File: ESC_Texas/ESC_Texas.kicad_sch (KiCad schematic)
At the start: 78 parts, among them IC1 nRF52840-QFAA-F-R7, IC11 LM3480IM3-3.3_NOPB, IC12 LM3480IM3-3.3_NOPB, J1 RJ45, J11 Battery+, J12 Conn_01x02, J13 Conn_01x04_Pin, J14 Conn_01x01_Pin, J15 Conn_01x01_Pin, J16 Conn_01x01_Pin, J17 Conn_01x01_Pin, J2 BD125-10-A-0305-0580-L-B, J3 Motor, J4 Conn_01x02_Pin, P0.03 TestPoint, P0.10 TestPoint, P0.11 TestPoint, P0.12 TestPoint, P0.7 TestPoint, P0.9 TestPoint, P1.0 TestPoint, P1.1 TestPoint, P1.9 TestPoint, U1 MCP2515-xSO, U2 TJA1051T, X1 CM7V-T1A-32.768kHz, X2 32MHz, X3 C115962

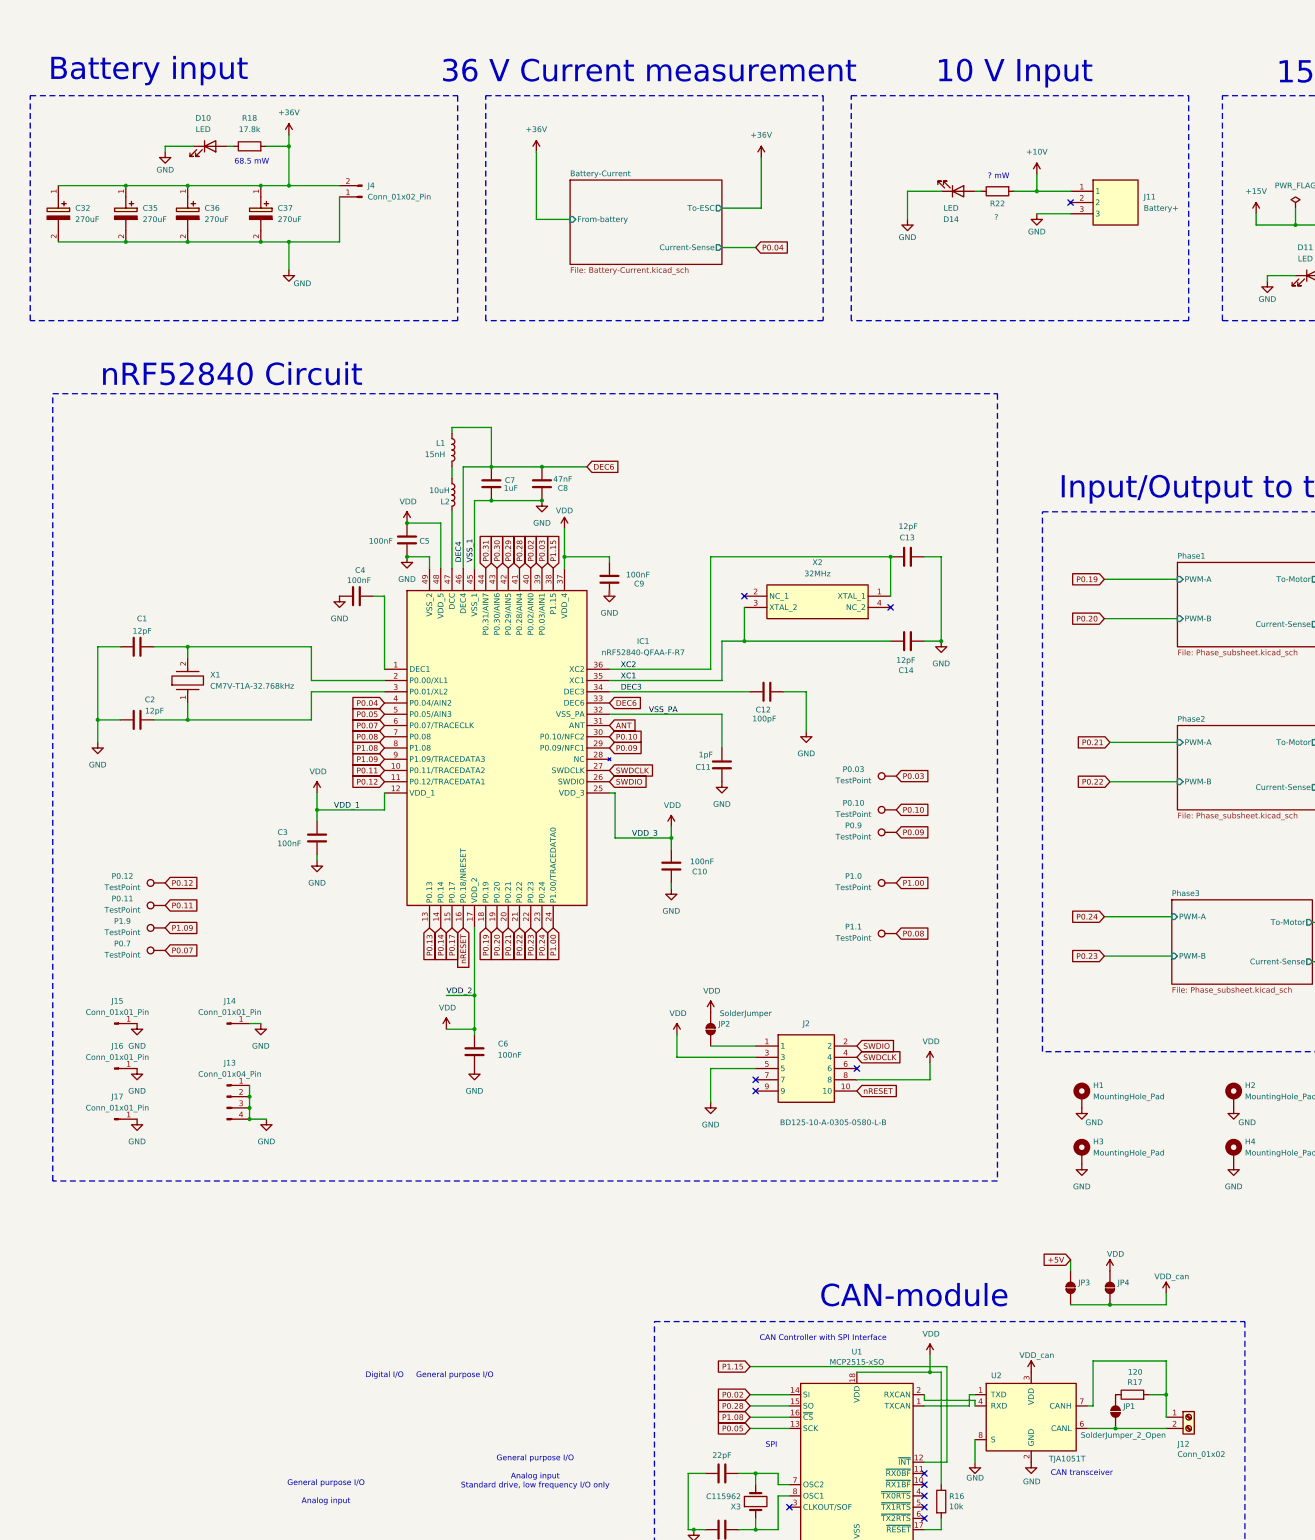
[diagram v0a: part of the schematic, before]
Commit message: Added combined CAN and 10v connector
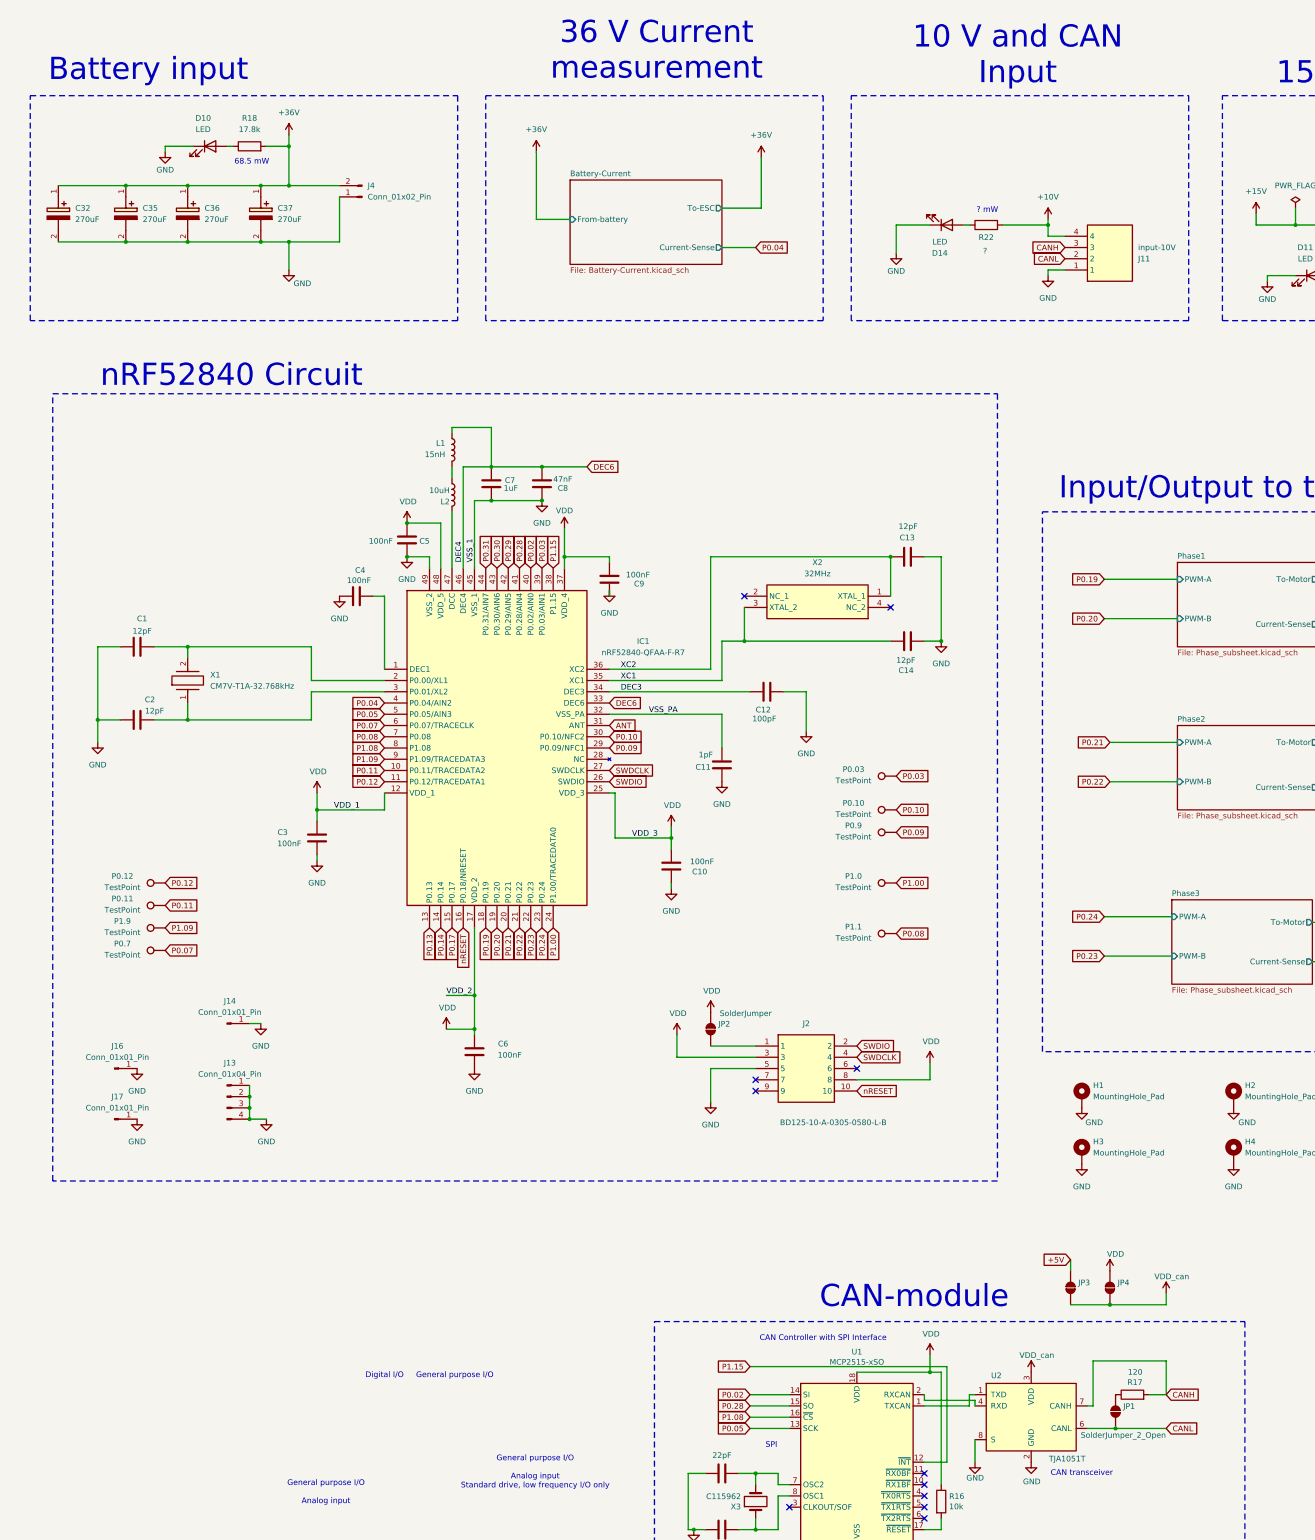
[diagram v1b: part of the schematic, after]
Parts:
- removed J12: Conn_01x02, Connector_Phoenix_MC:PhoenixContact_MCV_1,5_2-G-3.5_1x02_P3.50mm_Vertical, symbol Connector:Screw_Terminal_01x02
- removed J15: Conn_01x01_Pin, Connector_PinHeader_2.54mm:PinHeader_1x01_P2.54mm_Vertical, symbol Connector:Conn_01x01_Pin
- J11: value Battery+ -> input-10V; footprint LIB_2350514-3:SHDRRA3W90P0X350_1X3_1110X920X691P -> TBP02R1-381-04BE:TBP02R1-381-02BE
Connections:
- net +10V: now also J11.4; no longer J11.1
- net GND: now also J11.1; no longer J11.3
- net CANL: now reaches JP1.2 (B), U2.6 (CANL)
- net CANL: now also J11.2
- net CANH: now reaches R17.2, U2.7 (CANH)
- net CANH: now also J11.3
- no-connect marks 12 -> 11
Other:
- note added: "10 V and CAN Input"
- note removed: "10 V Input"
- moved on the sheet: D14, R22

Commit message: saved project
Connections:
- net +10V: now also J11.1; no longer J11.4
- net CANH: now also J11.2; no longer J11.3
- net CANL: now also J11.3; no longer J11.2
- net GND: now also J11.4; no longer J11.1
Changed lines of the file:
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@@
-	)
-	(symbol
-		(lib_name "2350514-3_1")
-		(lib_id "2350514-3:2350514-3")
-		(at 270.51 73.66 0)
-		(mirror x)
-		(unit 1)
-		(exclude_from_sim no)
-		(in_bom yes)
-		(on_board yes)
-		(dnp no)
-		(property "Reference" "J11"
-			(at 287.02 71.1201 0)
-			(effects
-				(font
-					(size 1.27 1.27)
-				)
-				(justify left)
-			)
-		)
-		(property "Value" "input-10V"
-			(at 287.02 68.5801 0)
-			(effects
-				(font
-					(size 1.27 1.27)
-				)
-				(justify left)
-			)
-		)
-		(property "Footprint" "TBP02R1-381-04BE:TBP02R1-381-02BE"
-			(at 287.02 -21.26 0)
-			(effects
-				(font
-					(size 1.27 1.27)
-				)
-				(justify left top)
-				(hide yes)
-			)
-		)
-		(property "Datasheet" "https://www.te.com/commerce/DocumentDelivery/DDEController?Action=srchrtrv&DocNm=3-1773982-8&DocType=Data%20Sheet&DocLang=English&PartCntxt=2350514-3&DocFormat=pdf"
-			(at 287.02 -121.26 0)
-			(effects
-				(font
-					(size 1.27 1.27)
-				)
-				(justify left top)
-				(hide yes)
-			)
-		)
-		(property "Description" "Body Features: Primary Product Color Green | Product Orientation Right Angle | Configuration Features: Stacking Configuration Side Stackable | Number of Rows 1 | Number of Positions 3 | Contact Features: Contact Mating Area Plating Material Tin | Contact Current Rating (Max) 10 AMP | Contact Base Material Brass | Electrical Characteristics: Operating Voltage 300 VAC | Housing Features: Housing Material PA 66 | Centerline (Pitch) .137 INCH | Centerline (Pitch) 3.5 MM | Mechanical Attachment: Connector Mounti"
-			(at 270.002 93.726 0)
-			(effects
-				(font
-					(size 1.27 1.27)
-				)
-				(hide yes)
-			)
-		)
-		(property "Height" "6.91"
-			(at 287.02 -321.26 0)
-			(effects
-				(font
-					(size 1.27 1.27)
-				)
-				(justify left top)
-				(hide yes)
-			)
-		)
-		(property "Farnell Part Number" ""
-			(at 287.02 -421.26 0)
-			(effects
-				(font
-					(size 1.27 1.27)
-				)
-				(justify left top)
-				(hide yes)
-			)
-		)
-		(property "Farnell Price/Stock" ""
-			(at 287.02 -521.26 0)
-			(effects
-				(font
-					(size 1.27 1.27)
-				)
-				(justify left top)
-				(hide yes)
-			)
-		)
-		(property "Manufacturer_Name" "TE Connectivity"
-			(at 287.02 -621.26 0)
-			(effects
-				(font
-					(size 1.27 1.27)
-				)
-				(justify left top)
-				(hide yes)
-			)
-		)
-		(property "Manufacturer_Part_Number" "2350514-3"
-			(at 287.02 -721.26 0)
-			(effects
-				(font
-					(size 1.27 1.27)
-				)
-				(justify left top)
-				(hide yes)
-			)
-		)
-		(pin "3"
-		)
-		(pin "2"
-		)
-		(pin "1"
-		)
-		(pin "4"
-		)
-		(instances
-			(project "ESC_Texas"
-				(path "/0e3a5351-d2cd-4ecc-a1be-cca9c5f62ea0"
-					(reference "J11")
-					(unit 1)
-				)
-			)
-		)
 	)
 	(symbol
@@
 					(unit 1)
 				)
+			)
+		)
+	)
+	(symbol
+		(lib_name "2350514-3_1")
+		(lib_id "2350514-3:2350514-3")
+		(at 270.51 66.04 0)
+		(unit 1)
+		(exclude_from_sim no)
+		(in_bom yes)
+		(on_board yes)
+		(dnp no)
+		(property "Reference" "J11"
+			(at 287.02 68.5799 0)
+			(effects
+				(font
+					(size 1.27 1.27)
+				)
+				(justify left)
+			)
+		)
+		(property "Value" "input-10V"
+			(at 287.02 71.1199 0)
+			(effects
+				(font
+					(size 1.27 1.27)
+				)
+				(justify left)
+			)
+		)
+		(property "Footprint" "TBP02R1-381-04BE:TBP02R1-381-02BE"
+			(at 287.02 160.96 0)
+			(effects
+				(font
+					(size 1.27 1.27)
+				)
+				(justify left top)
+				(hide yes)
+			)
+		)
+		(property "Datasheet" "https://www.te.com/commerce/DocumentDelivery/DDEController?Action=srchrtrv&DocNm=3-1773982-8&DocType=Data%20Sheet&DocLang=English&PartCntxt=2350514-3&DocFormat=pdf"
+			(at 287.02 260.96 0)
+			(effects
+				(font
+					(size 1.27 1.27)
+				)
+				(justify left top)
+				(hide yes)
+			)
+		)
+		(property "Description" "Body Features: Primary Product Color Green | Product Orientation Right Angle | Configuration Features: Stacking Configuration Side Stackable | Number of Rows 1 | Number of Positions 3 | Contact Features: Contact Mating Area Plating Material Tin | Contact Current Rating (Max) 10 AMP | Contact Base Material Brass | Electrical Characteristics: Operating Voltage 300 VAC | Housing Features: Housing Material PA 66 | Centerline (Pitch) .137 INCH | Centerline (Pitch) 3.5 MM | Mechanical Attachment: Connector Mounti"
+			(at 270.002 45.974 0)
+			(effects
+				(font
+					(size 1.27 1.27)
+				)
+				(hide yes)
+			)
+		)
+		(property "Height" "6.91"
+			(at 287.02 460.96 0)
+			(effects
+				(font
+					(size 1.27 1.27)
+				)
+				(justify left top)
+				(hide yes)
+			)
+		)
+		(property "Farnell Part Number" ""
+			(at 287.02 560.96 0)
+			(effects
+				(font
+					(size 1.27 1.27)
+				)
+				(justify left top)
+				(hide yes)
+			)
+		)
+		(property "Farnell Price/Stock" ""
+			(at 287.02 660.96 0)
+			(effects
+				(font
+					(size 1.27 1.27)
+				)
+				(justify left top)
+				(hide yes)
+			)
+		)
+		(property "Manufacturer_Name" "TE Connectivity"
+			(at 287.02 760.96 0)
+			(effects
+				(font
+					(size 1.27 1.27)
+				)
+				(justify left top)
+				(hide yes)
+			)
+		)
+		(property "Manufacturer_Part_Number" "2350514-3"
+			(at 287.02 860.96 0)
+			(effects
+				(font
+					(size 1.27 1.27)
+				)
+				(justify left top)
+				(hide yes)
+			)
+		)
+		(pin "3"
+		)
+		(pin "2"
+		)
+		(pin "1"
+		)
+		(pin "4"
+		)
+		(instances
+			(project "ESC_Texas"
+				(path "/0e3a5351-d2cd-4ecc-a1be-cca9c5f62ea0"
+					(reference "J11")
+					(unit 1)
+				)

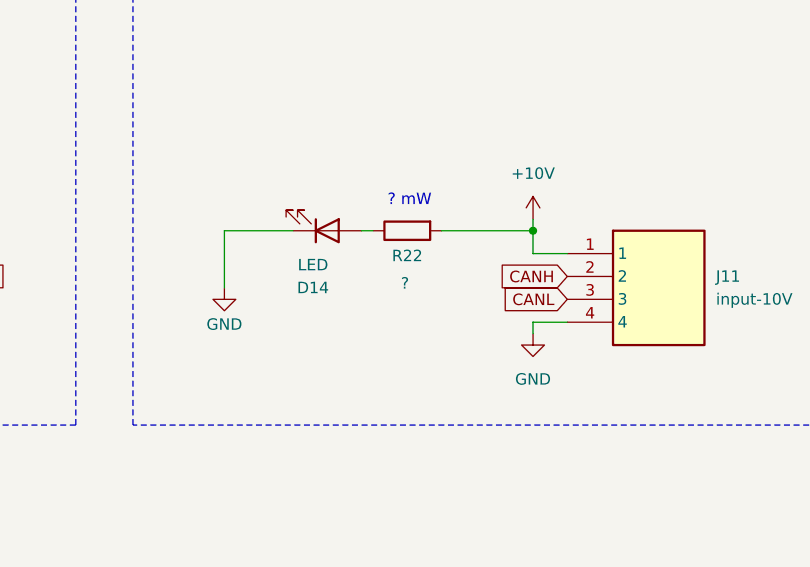
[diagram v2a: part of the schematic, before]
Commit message: moved a trace
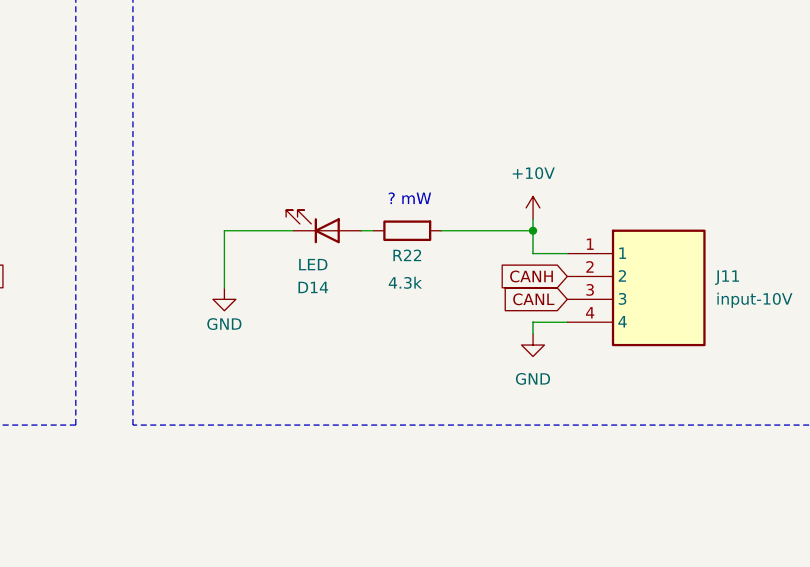
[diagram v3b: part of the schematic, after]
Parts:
- R22: value ? -> 4.3k
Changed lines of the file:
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@@
 			)
 		)
-		(property "Value" "?"
+		(property "Value" "4.3k"
 			(at 252.476 69.342 90)
 			(effects

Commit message: Changed hall connector
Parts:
- removed J1: RJ45, Connector_RJ:RJ45_Amphenol_54602-x08_Horizontal, symbol Connector:RJ45
- removed J16: Conn_01x01_Pin, Connector_PinHeader_2.54mm:PinHeader_1x01_P2.54mm_Vertical, symbol Connector:Conn_01x01_Pin
- added C47, C48, C49: F, Capacitor_SMD:C_0805_2012Metric, symbol Device:C
- added C51: 330n, Capacitor_SMD:C_0805_2012Metric, symbol Device:C
- added IC16: MC78L05ACHT1G, MC78L05ACHT1G:MC78L05ACHX_1, symbol MC78L05ACHT1G:MC78L05ACHT1G
- added J12: Hall Effect, TJ0631530000G:TJ0631530000G, symbol TJ0631530000G:TJ0631530000G
- added R28, R29, R30: R, Resistor_SMD:R_0805_2012Metric, symbol Device:R
- renumbered P1.1 to P0.08, P0.9 to P0.09
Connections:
- net +15V: now also C51.2, IC16.3 (VIN)
- net +5V: now also IC16.1 (VOUT)
- net GND: now also C47.2, C48.2, C49.2, C51.1, IC16.2 (GND), IC16.4 (TAB), J12.1
- net P0.13: now also C49.1, R28.1
- net P0.14: now also C47.1, R29.1
- net P0.17: now also C48.1, R30.1
- net VDD: now also J12.6
- net at SpeedTemp1.1: now also J12.2
- new net: J12.3, R30.2
- new net: J12.4, R29.2
- new net: J12.5, R28.2
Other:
- note added: "5 V regulator"
- moved on the sheet: C33, C34, C40, C41, D12, D13, H1, H2, H3, H4, IC11, IC12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
